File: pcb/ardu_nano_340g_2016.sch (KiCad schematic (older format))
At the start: 35 parts, among them J1 USB_B_Mini, J2 Conn_01x15, J3 Conn_01x15, J4 Conn_02x03_Odd_Even, U1 CH340G-JEC, U2 ATMEGA328P-AU, U3 LM1117-5.0, Y1 Resonator, Y2 Resonator

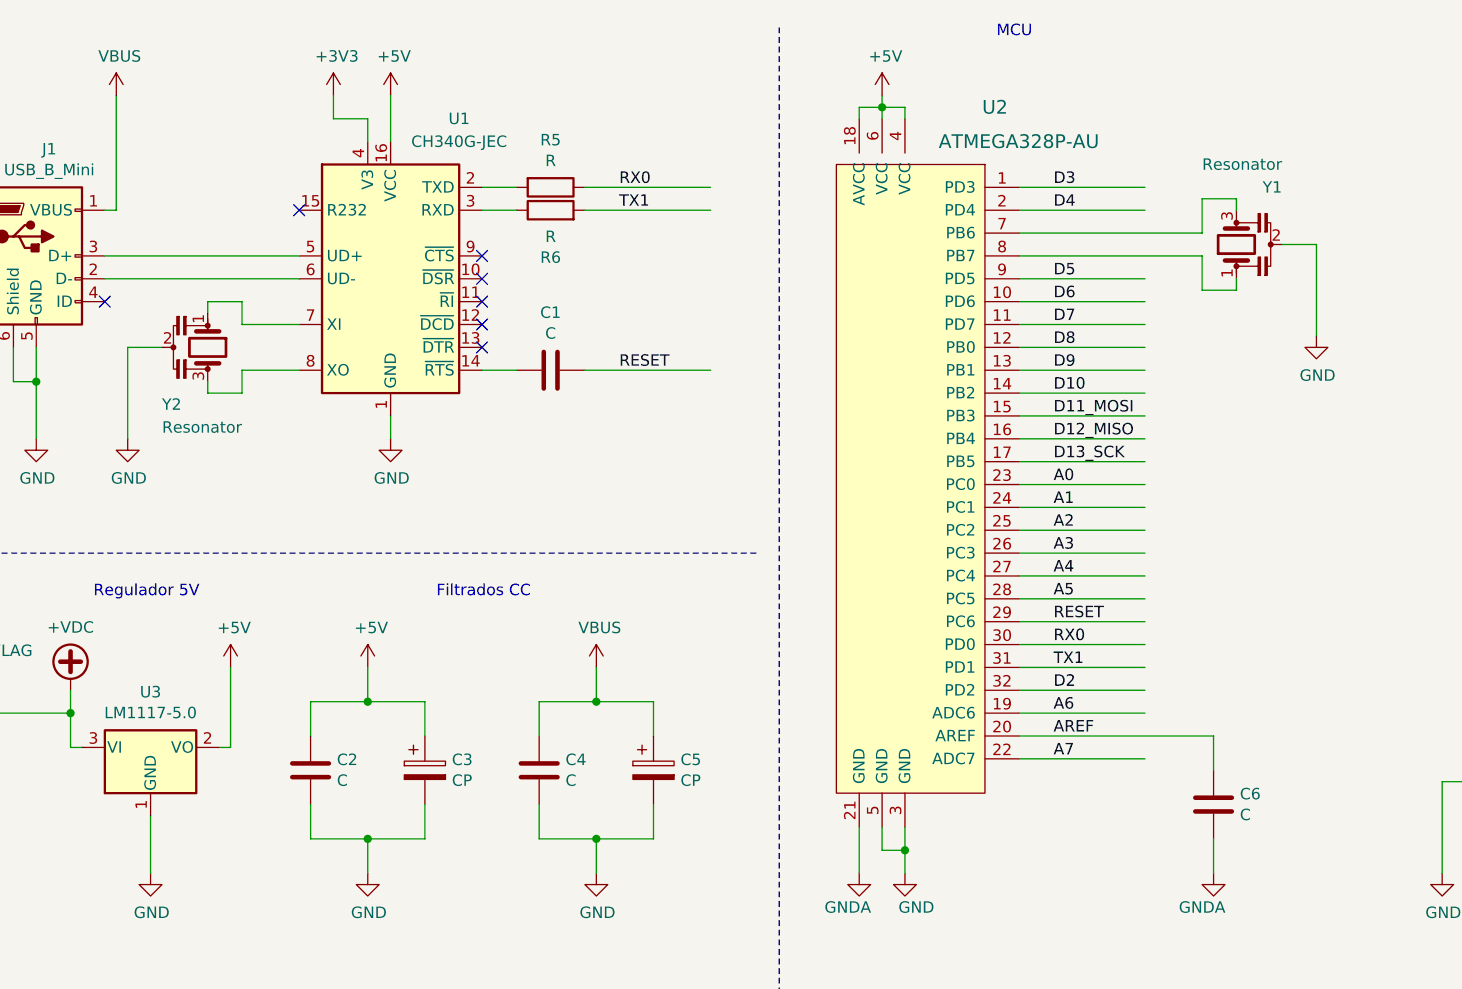
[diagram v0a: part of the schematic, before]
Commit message: se agregaron valores y codigos de compra de todas las partes
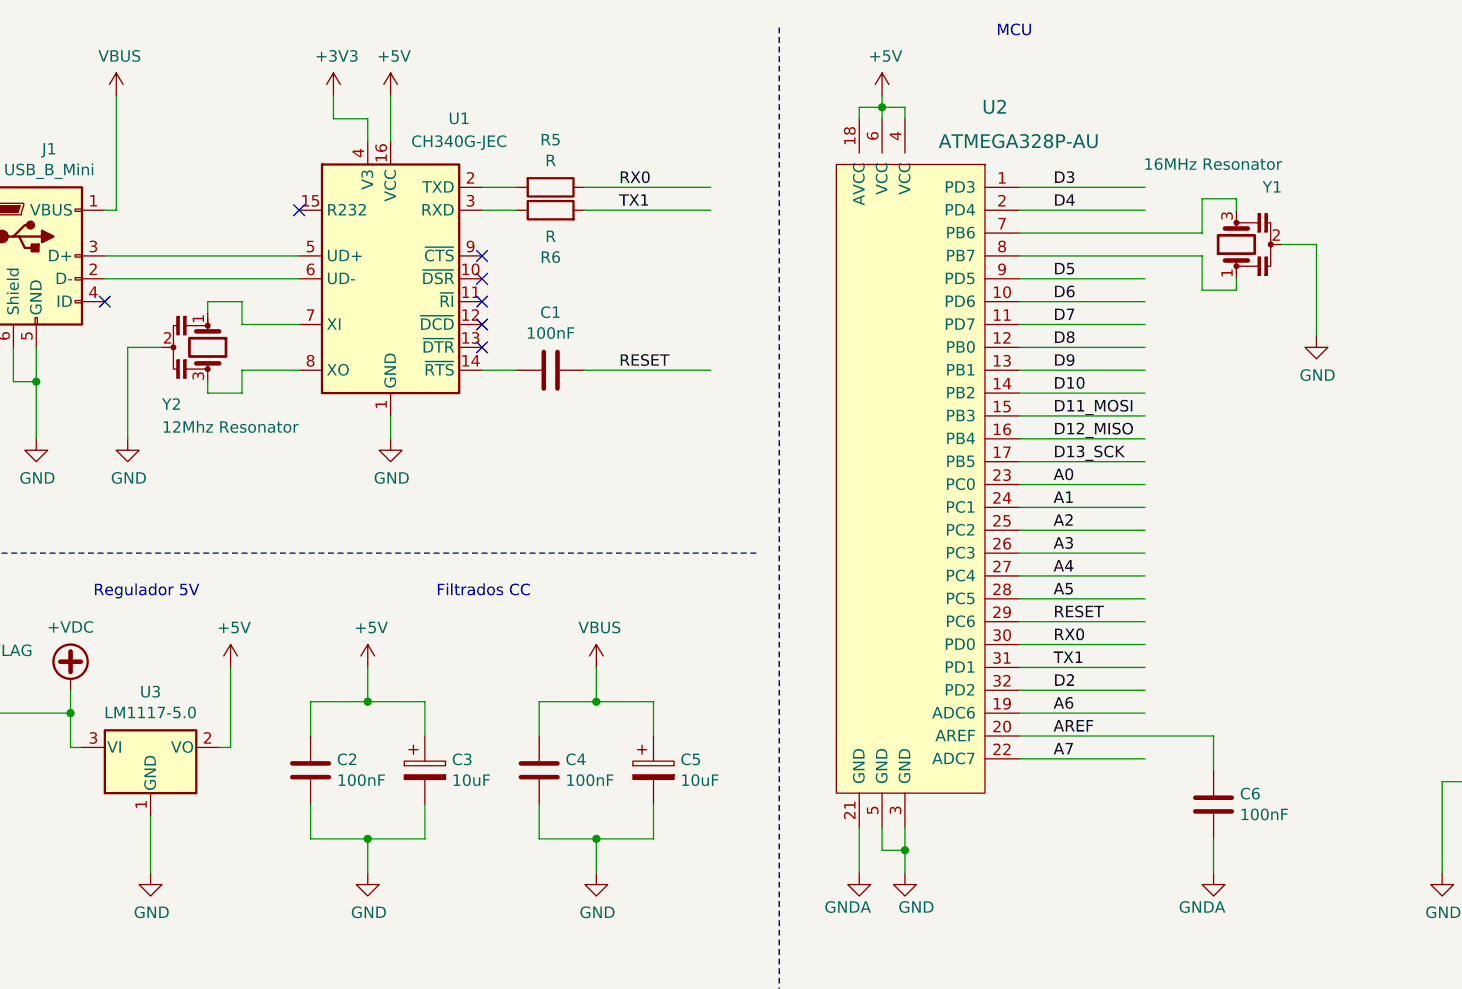
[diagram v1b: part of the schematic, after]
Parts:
- C1, C2, C4, C6: value C -> 100nF; DK_Detail_Page (none) -> https://www.digikey.com/en/products/detail/samsung-electro-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; Digi-Key_PN (none) -> 1276-CL21B104KBFXPJECT-ND; MPN (none) -> CL21B104KBFXPJE; Manufacturer (none) -> SAMSUNG ELECTRO-MECHANICS
- C3, C5: value CP -> 10uF; DK_Detail_Page (none) -> https://lcsc.com/product-detail/Others_AVX_TCJA106M016R0200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; Digi-Key_PN (none) -> C194304; MPN (none) -> https://lcsc.com/product-detail/Others_AVX_TCJA106M016R0200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; Manufacturer (none) -> AVX
- D1: DK_Detail_Page (none) -> https://www.digikey.com/en/products/detail/w%C3%BCrth-elekt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; Digi-Key_PN (none) -> 732-4985-1-ND; MPN (none) -> 150080SS75000; Manufacturer (none) -> Würth Elektronik
- D2, D3: DK_Detail_Page (none) -> https://www.digikey.com/en/products/detail/w%C3%BCrth-elekt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; Digi-Key_PN (none) -> 732-4986-1-ND; MPN (none) -> 150080VS75000; Manufacturer (none) -> Würth Elektronik
- D4: DK_Detail_Page (none) -> https://www.digikey.com/en/products/detail/w%C3%BCrth-elekt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; Digi-Key_PN (none) -> 732-4987-1-ND; MPN (none) -> 150080YS75000; Manufacturer (none) -> Würth Elektronik
- D5: DK_Detail_Page (none) -> https://lcsc.com/product-detail/Others_Vishay-Intertech_SD1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; Digi-Key_PN (none) -> C241955; MPN (none) -> SD101CWS; Manufacturer (none) -> Vishay
- J1: footprint (none) -> digikey-footprints:USB_Mini_B_Female_UX60-MB-5ST; DK_Datasheet_Link (none) -> https://media.digikey.com/pdf/Data%20Sheets/Hirose%20PDFs/U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; DK_Detail_Page (none) -> https://www.digikey.com/en/products/detail/hirose-electric-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; Description (none) -> CONN RCPT USB2.0 MINI B SMD R/A; Digi-Key_PN (none) -> H2959CT-ND; Family (none) -> USB, DVI, HDMI Connectors; MPN (none) -> UX60-MB-5ST; Manufacturer (none) -> Hirose Electric Co Ltd; Status (none) -> Active
- J2, J3: DK_Detail_Page (none) -> https://www.digikey.com/en/products/detail/samtec-inc/TSW-1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; Digi-Key_PN (none) -> SAM1035-15-ND; MPN (none) -> TSW-115-07-T-S; Manufacturer (none) -> Samtec Inc.
- J4: DK_Detail_Page (none) -> https://www.digikey.com/en/products/detail/samtec-inc/TSW-1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; Digi-Key_PN (none) -> SAM1034-03-ND; MPN (none) -> TSW-103-07-T-D; Manufacturer (none) -> Samtec Inc.
- R1, R2, R3, R4, R7: footprint (none) -> Resistor_SMD:R_0805_2012Metric_Pad1.15x1.40mm_HandSolder; DK_Detail_Page (none) -> https://www.digikey.com/en/products/detail/stackpole-electr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; Digi-Key_PN (none) -> RNCP0805FTD1K00CT-ND; MPN (none) -> RNCP0805FTD1K00; Manufacturer (none) -> Stackpole Electronics Inc
- R5, R6: DK_Detail_Page (none) -> https://www.digikey.com/en/products/detail/stackpole-electr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; Digi-Key_PN (none) -> RNCP0805FTD1K00CT-ND; MPN (none) -> RNCP0805FTD1K00; Manufacturer (none) -> Stackpole Electronics Inc
- S1: DK_Detail_Page /product-detail/en/omron-electronics-inc-emc-div/B3U-1000P/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 -> https://www.digikey.com/en/products/detail/omron-electronic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
- U1: DK_Detail_Page (none) -> https://lcsc.com/product-detail/USB-ICs_WCH-Jiangsu-Qin-Hen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; Digi-Key_PN (none) -> C14267; MPN (none) -> CH340G; Manufacturer (none) -> WCH(Jiangsu Qin Heng)
- U2: DK_Detail_Page /product-detail/en/microchip-technology/ATMEGA328P-AU/ATMEG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 -> https://www.digikey.com/en/products/detail/microchip-techno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
- U3: DK_Detail_Page (none) -> https://www.digikey.com/en/products/detail/texas-instrument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; Digi-Key_PN (none) -> LM1117MP-5.0/NOPBCT-ND; MPN (none) -> LM1117MP-5.0/NOPB; Manufacturer (none) -> Texas Instruments
- Y1: value Resonator -> 16MHz Resonator; footprint (none) -> Crystal:Resonator_SMD_muRata_CSTxExxV-3Pin_3.0x1.1mm_HandSoldering; DK_Detail_Page (none) -> https://www.digikey.de/product-detail/en/murata-electronics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; Digi-Key_PN (none) -> 490-17948-1-ND; MPN (none) -> CSTNE16M0V530000R0; Manufacturer (none) -> Murata Electronics
- Y2: value Resonator -> 12Mhz Resonator; footprint (none) -> Crystal:Resonator_SMD_muRata_CSTxExxV-3Pin_3.0x1.1mm_HandSoldering; DK_Detail_Page (none) -> https://www.digikey.de/product-detail/en/murata-electronics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; Digi-Key_PN (none) -> 490-17943-1-ND; MPN (none) -> CSTNE12M0G550000R0; Manufacturer (none) -> Murata Electronics

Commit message: asignacion de todas las huellas
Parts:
- H1, H2, H3, H4: footprint MountingHole:MountingHole_3.2mm_M3_ISO14580 -> MountingHole:MountingHole_2.2mm_M2_ISO14580
- J1: footprint digikey-footprints:USB_Mini_B_Female_UX60-MB-5ST -> Connector_USB:USB_Mini-B_Wuerth_65100516121_Horizontal
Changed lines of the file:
@@
 F 0 "J1" H 1157 2167 50  0000 C CNN
 F 1 "USB_B_Mini" H 1157 2076 50  0000 C CNN
-F 2 "digikey-footprints:USB_Mini_B_Female_UX60-MB-5ST" H 1250 1650 50  0001 C CNN
+F 2 "Connector_USB:USB_Mini-B_Wuerth_65100516121_Horizontal" H 1250 1650 50  0001 C CNN
 F 3 "https://media.digikey.com/pdf/Data%20Sheets/Hirose%20PDFs/UX%20Series.pdf" H 1250 1650 50  0001 C CNN
 F 4 "https://media.digikey.com/pdf/Data%20Sheets/Hirose%20PDFs/UX%20Series.pdf" H 1100 1700 50  0001 C CNN "DK_Datasheet_Link"
@@
 F 0 "H1" H 7200 6396 50  0000 L CNN
 F 1 "MountingHole" H 7200 6305 50  0000 L CNN
-F 2 "MountingHole:MountingHole_3.2mm_M3_ISO14580" H 7100 6350 50  0001 C CNN
+F 2 "MountingHole:MountingHole_2.2mm_M2_ISO14580" H 7100 6350 50  0001 C CNN
 F 3 "~" H 7100 6350 50  0001 C CNN
 	1    7100 6350
@@
 F 0 "H2" H 8000 6396 50  0000 L CNN
 F 1 "MountingHole" H 8000 6305 50  0000 L CNN
-F 2 "MountingHole:MountingHole_3.2mm_M3_ISO14580" H 7900 6350 50  0001 C CNN
+F 2 "MountingHole:MountingHole_2.2mm_M2_ISO14580" H 7900 6350 50  0001 C CNN
 F 3 "~" H 7900 6350 50  0001 C CNN
 	1    7900 6350
@@
 F 0 "H3" H 8800 6396 50  0000 L CNN
 F 1 "MountingHole" H 8800 6305 50  0000 L CNN
-F 2 "MountingHole:MountingHole_3.2mm_M3_ISO14580" H 8700 6350 50  0001 C CNN
+F 2 "MountingHole:MountingHole_2.2mm_M2_ISO14580" H 8700 6350 50  0001 C CNN
 F 3 "~" H 8700 6350 50  0001 C CNN
 	1    8700 6350
@@
 F 0 "H4" H 9600 6396 50  0000 L CNN
 F 1 "MountingHole" H 9600 6305 50  0000 L CNN
-F 2 "MountingHole:MountingHole_3.2mm_M3_ISO14580" H 9500 6350 50  0001 C CNN
+F 2 "MountingHole:MountingHole_2.2mm_M2_ISO14580" H 9500 6350 50  0001 C CNN
 F 3 "~" H 9500 6350 50  0001 C CNN
 	1    9500 6350

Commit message: Se actualizo a version 2.1 porque se agrego capacitor de filtrado de 3V3
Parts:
- added C7: 100nF, Capacitor_SMD:C_0805_2012Metric_Pad1.15x1.40mm_HandSolder, symbol Device:C
- J1: symbol Connector:USB_B_Mini -> ardu_nano_340g_2016-rescue:USB_B_Mini-Connector
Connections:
- wire segments 175 -> 177
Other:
- moved on the sheet: C2, C3, C4, C5, C6, D1, D2, D3, D4, D5, J2, J3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

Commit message: primera acomodad en el PCB, faltan un par de 3D y una revision general del posicionamiento
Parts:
- C7: footprint Capacitor_SMD:C_0805_2012Metric_Pad1.15x1.40mm_HandSolder -> Capacitor_SMD:C_0805_2012Metric_Pad1.18x1.45mm_HandSolder
- NT1: footprint NetTie:NetTie-2_SMD_Pad2.0mm -> NetTie:NetTie-2_SMD_Pad0.5mm
- U2: footprint digikey-footprints:TQFP-32_7x7mm -> Package_QFP:LQFP-32_7x7mm_P0.8mm
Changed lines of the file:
@@
 F 0 "U2" H 5100 4350 60  0000 L CNN
 F 1 "ATMEGA328P-AU" H 4700 4200 60  0000 L CNN
-F 2 "digikey-footprints:TQFP-32_7x7mm" H 5750 2900 60  0001 L CNN
+F 2 "Package_QFP:LQFP-32_7x7mm_P0.8mm" H 5750 2900 60  0001 L CNN
 F 3 "http://www.microchip.com/mymicrochip/filehandler.aspx?ddocname=en608326" H 5750 3000 60  0001 L CNN
 F 4 "ATMEGA328P-AU-ND" H 5750 3100 60  0001 L CNN "Digi-Key_PN"
@@
 F 0 "NT1" H 3950 6931 50  0000 C CNN
 F 1 "Net-Tie_2" H 3950 6840 50  0000 C CNN
-F 2 "NetTie:NetTie-2_SMD_Pad2.0mm" H 3950 6750 50  0001 C CNN
+F 2 "NetTie:NetTie-2_SMD_Pad0.5mm" H 3950 6750 50  0001 C CNN
 F 3 "~" H 3950 6750 50  0001 C CNN
 	1    3950 6750
@@
 F 0 "C7" H 4615 3996 50  0000 L CNN
 F 1 "100nF" H 4615 3905 50  0000 L CNN
-F 2 "Capacitor_SMD:C_0805_2012Metric_Pad1.15x1.40mm_HandSolder" H 4538 3800 50  0001 C CNN
+F 2 "Capacitor_SMD:C_0805_2012Metric_Pad1.18x1.45mm_HandSolder" H 4538 3800 50  0001 C CNN
 F 3 "http://product.samsungsem.com/mlcc/CL21B104KBFXPJ.do" H 4500 3950 50  0001 C CNN
 F 4 "https://www.digikey.com/en/products/detail/samsung-electro-mechanics/CL21B104KBFXPJE/11487741" H 4500 3950 50  0001 C CNN "DK_Detail_Page"

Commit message: Se agregaron valores de resistencias e imagenes de placa real de referencia
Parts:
- R1, R2, R3, R4, R5, R6: value R -> 1k
- R7: value R -> 10k
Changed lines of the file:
@@
 P 3350 1400
 F 0 "R5" V 3143 1400 50  0000 C CNN
-F 1 "R" V 3234 1400 50  0000 C CNN
+F 1 "1k" V 3234 1400 50  0000 C CNN
 F 2 "Resistor_SMD:R_0805_2012Metric_Pad1.15x1.40mm_HandSolder" V 3280 1400 50  0001 C CNN
 F 3 "https://www.seielect.com/catalog/sei-rncp.pdf" H 3350 1400 50  0001 C CNN
@@
 P 3350 1500
 F 0 "R6" V 3143 1500 50  0000 C CNN
-F 1 "R" V 3234 1500 50  0000 C CNN
+F 1 "1k" V 3234 1500 50  0000 C CNN
 F 2 "Resistor_SMD:R_0805_2012Metric_Pad1.15x1.40mm_HandSolder" V 3280 1500 50  0001 C CNN
 F 3 "https://www.seielect.com/catalog/sei-rncp.pdf" H 3350 1500 50  0001 C CNN
@@
 P 8050 1300
 F 0 "R1" H 8120 1346 50  0000 L CNN
-F 1 "R" H 8120 1255 50  0000 L CNN
+F 1 "1k" H 8120 1255 50  0000 L CNN
 F 2 "Resistor_SMD:R_0805_2012Metric_Pad1.15x1.40mm_HandSolder" V 7980 1300 50  0001 C CNN
 F 3 "https://www.seielect.com/catalog/sei-rncp.pdf" H 8050 1300 50  0001 C CNN
@@
 P 8800 1300
 F 0 "R2" H 8870 1346 50  0000 L CNN
-F 1 "R" H 8870 1255 50  0000 L CNN
+F 1 "1k" H 8870 1255 50  0000 L CNN
 F 2 "Resistor_SMD:R_0805_2012Metric_Pad1.15x1.40mm_HandSolder" V 8730 1300 50  0001 C CNN
 F 3 "https://www.seielect.com/catalog/sei-rncp.pdf" H 8800 1300 50  0001 C CNN
@@
 P 9550 1300
 F 0 "R3" H 9620 1346 50  0000 L CNN
-F 1 "R" H 9620 1255 50  0000 L CNN
+F 1 "1k" H 9620 1255 50  0000 L CNN
 F 2 "Resistor_SMD:R_0805_2012Metric_Pad1.15x1.40mm_HandSolder" V 9480 1300 50  0001 C CNN
 F 3 "https://www.seielect.com/catalog/sei-rncp.pdf" H 9550 1300 50  0001 C CNN
@@
 P 10300 1300
 F 0 "R4" H 10370 1346 50  0000 L CNN
-F 1 "R" H 10370 1255 50  0000 L CNN
+F 1 "1k" H 10370 1255 50  0000 L CNN
 F 2 "Resistor_SMD:R_0805_2012Metric_Pad1.15x1.40mm_HandSolder" V 10230 1300 50  0001 C CNN
 F 3 "https://www.seielect.com/catalog/sei-rncp.pdf" H 10300 1300 50  0001 C CNN
@@
 P 6000 6050
 F 0 "R7" H 6070 6096 50  0000 L CNN
-F 1 "R" H 6070 6005 50  0000 L CNN
+F 1 "10k" H 6070 6005 50  0000 L CNN
 F 2 "Resistor_SMD:R_0805_2012Metric_Pad1.15x1.40mm_HandSolder" V 5930 6050 50  0001 C CNN
 F 3 "https://www.seielect.com/catalog/sei-rncp.pdf" H 6000 6050 50  0001 C CNN

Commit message: V2.2 Se agregó capacitor desacople IC USB y se redujo huella resonadores
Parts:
- added C8: 100nF, Capacitor_SMD:C_0805_2012Metric_Pad1.18x1.45mm_HandSolder, symbol Device:C
- H1, H2: footprint MountingHole:MountingHole_2.2mm_M2_ISO14580 -> MountingHole:MountingHole_2.2mm_M2_ISO7380
- Y1, Y2: footprint Crystal:Resonator_SMD_muRata_CSTxExxV-3Pin_3.0x1.1mm_HandSoldering -> Crystal:Resonator_SMD_muRata_CSTxExxV-3Pin_3.0x1.1mm
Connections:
- wire segments 177 -> 179
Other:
- note added: "Desacople IC USB"
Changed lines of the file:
@@
 F 0 "Y2" V 2100 1900 50  0000 L CNN
 F 1 "12Mhz Resonator" V 2200 1900 50  0000 L CNN
-F 2 "Crystal:Resonator_SMD_muRata_CSTxExxV-3Pin_3.0x1.1mm_HandSoldering" H 1825 2100 50  0001 C CNN
+F 2 "Crystal:Resonator_SMD_muRata_CSTxExxV-3Pin_3.0x1.1mm" H 1825 2100 50  0001 C CNN
 F 3 "https://www.murata.com/en-us/products/productdetail?partno=CSTNE12M0G550000R0" H 1825 2100 50  0001 C CNN
 F 4 "https://www.digikey.de/product-detail/en/murata-electronics/CSTNE12M0G550000R0/490-17943-1-ND/8747751" H 1850 2100 50  0001 C CNN "DK_Detail_Page"
@@
 F 0 "Y1" V 7250 1450 50  0000 L CNN
 F 1 "16MHz Resonator" V 7350 1450 50  0000 L CNN
-F 2 "Crystal:Resonator_SMD_muRata_CSTxExxV-3Pin_3.0x1.1mm_HandSoldering" H 6975 1650 50  0001 C CNN
+F 2 "Crystal:Resonator_SMD_muRata_CSTxExxV-3Pin_3.0x1.1mm" H 6975 1650 50  0001 C CNN
 F 3 "https://www.murata.com/en-us/products/productdetail?cate=cgsubResonators&partno=CSTNE16M0V530000R0" H 6975 1650 50  0001 C CNN
 F 4 "https://www.digikey.de/product-detail/en/murata-electronics/CSTNE16M0V530000R0/490-17948-1-ND/8747756" H 7000 1650 50  0001 C CNN "DK_Detail_Page"
@@
 F 0 "H1" H 7200 6396 50  0000 L CNN
 F 1 "MountingHole" H 7200 6305 50  0000 L CNN
-F 2 "MountingHole:MountingHole_2.2mm_M2_ISO14580" H 7100 6350 50  0001 C CNN
+F 2 "MountingHole:MountingHole_2.2mm_M2_ISO7380" H 7100 6350 50  0001 C CNN
 F 3 "~" H 7100 6350 50  0001 C CNN
 	1    7100 6350
@@
 F 0 "H2" H 8000 6396 50  0000 L CNN
 F 1 "MountingHole" H 8000 6305 50  0000 L CNN
-F 2 "MountingHole:MountingHole_2.2mm_M2_ISO14580" H 7900 6350 50  0001 C CNN
+F 2 "MountingHole:MountingHole_2.2mm_M2_ISO7380" H 7900 6350 50  0001 C CNN
 F 3 "~" H 7900 6350 50  0001 C CNN
 	1    7900 6350
@@
 Text Notes 8700 5400 0    50   ~ 0
 TIRA DE PINES A PROTO\n
+$Comp
+L Device:C C8
+U 1 1 5F8D5411
+P 4600 1700
+F 0 "C8" H 4715 1746 50  0000 L CNN
+F 1 "100nF" H 4715 1655 50  0000 L CNN
+F 2 "Capacitor_SMD:C_0805_2012Metric_Pad1.18x1.45mm_HandSolder" H 4638 1550 50  0001 C CNN
+F 3 "http://product.samsungsem.com/mlcc/CL21B104KBFXPJ.do" H 4600 1700 50  0001 C CNN
+F 4 "https://www.digikey.com/en/products/detail/samsung-electro-mechanics/CL21B104KBFXPJE/11487741" H 4600 1700 50  0001 C CNN "DK_Detail_Page"
+F 5 "1276-CL21B104KBFXPJECT-ND" H 4600 1700 50  0001 C CNN "Digi-Key_PN"
+F 6 "CL21B104KBFXPJE" H 4600 1700 50  0001 C CNN "MPN"
+F 7 "SAMSUNG ELECTRO-MECHANICS" H 4600 1700 50  0001 C CNN "Manufacturer"
+	1    4600 1700
+	1    0    0    -1
+$EndComp
+$Comp
+L power:GND #PWR040
+U 1 1 5F8D5417
+P 4600 2500
+F 0 "#PWR040" H 4600 2250 50  0001 C CNN
+F 1 "GND" H 4605 2327 50  0000 C CNN
+F 2 "" H 4600 2500 50  0001 C CNN
+F 3 "" H 4600 2500 50  0001 C CNN
+	1    4600 2500
+	1    0    0    -1
+$EndComp
+$Comp
+L power:+5V #PWR039
+U 1 1 5F8F61D2
+P 4600 1000
+F 0 "#PWR039" H 4600 850 50  0001 C CNN
+F 1 "+5V" H 4615 1173 50  0000 C CNN
+F 2 "" H 4600 1000 50  0001 C CNN
+F 3 "" H 4600 1000 50  0001 C CNN
+	1    4600 1000
+	1    0    0    -1
+$EndComp
+Wire Wire Line
+	4600 1000 4600 1550
+Wire Wire Line
+	4600 1850 4600 2500
+Wire Notes Line
+	4200 650  4200 2850
+Text Notes 4250 750  0    50   ~ 0
+Desacople IC USB
 $EndSCHEMATC
